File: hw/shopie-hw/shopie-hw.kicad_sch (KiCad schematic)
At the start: 4 parts, among them J1 Jack-DC, SW1 SW_SPDT

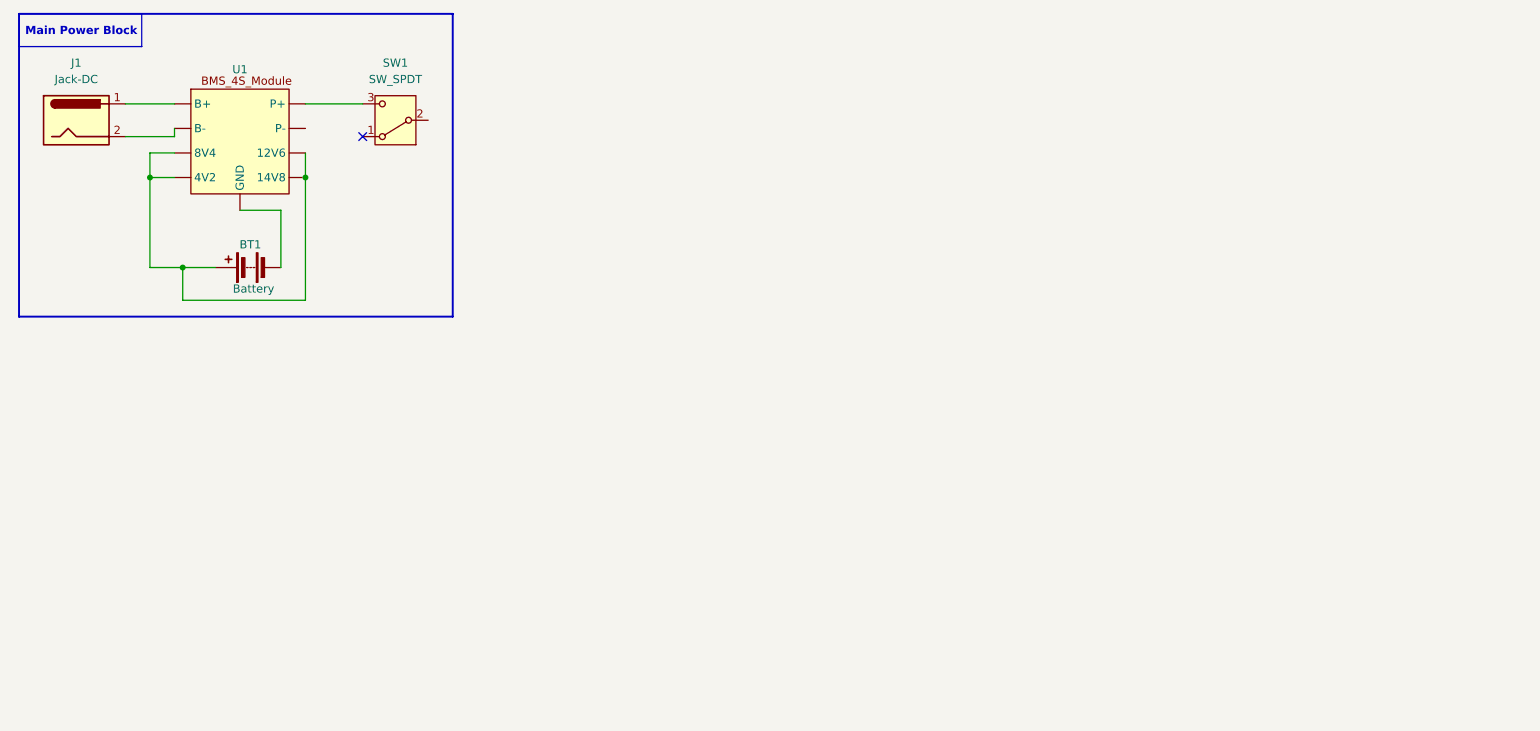
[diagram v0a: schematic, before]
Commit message: Add 5V and 3.3V voltage regulators to main power block
- Added switching regulator for 5V generation from VBAT
- Added LDO regulator for 3.3V output from 5V
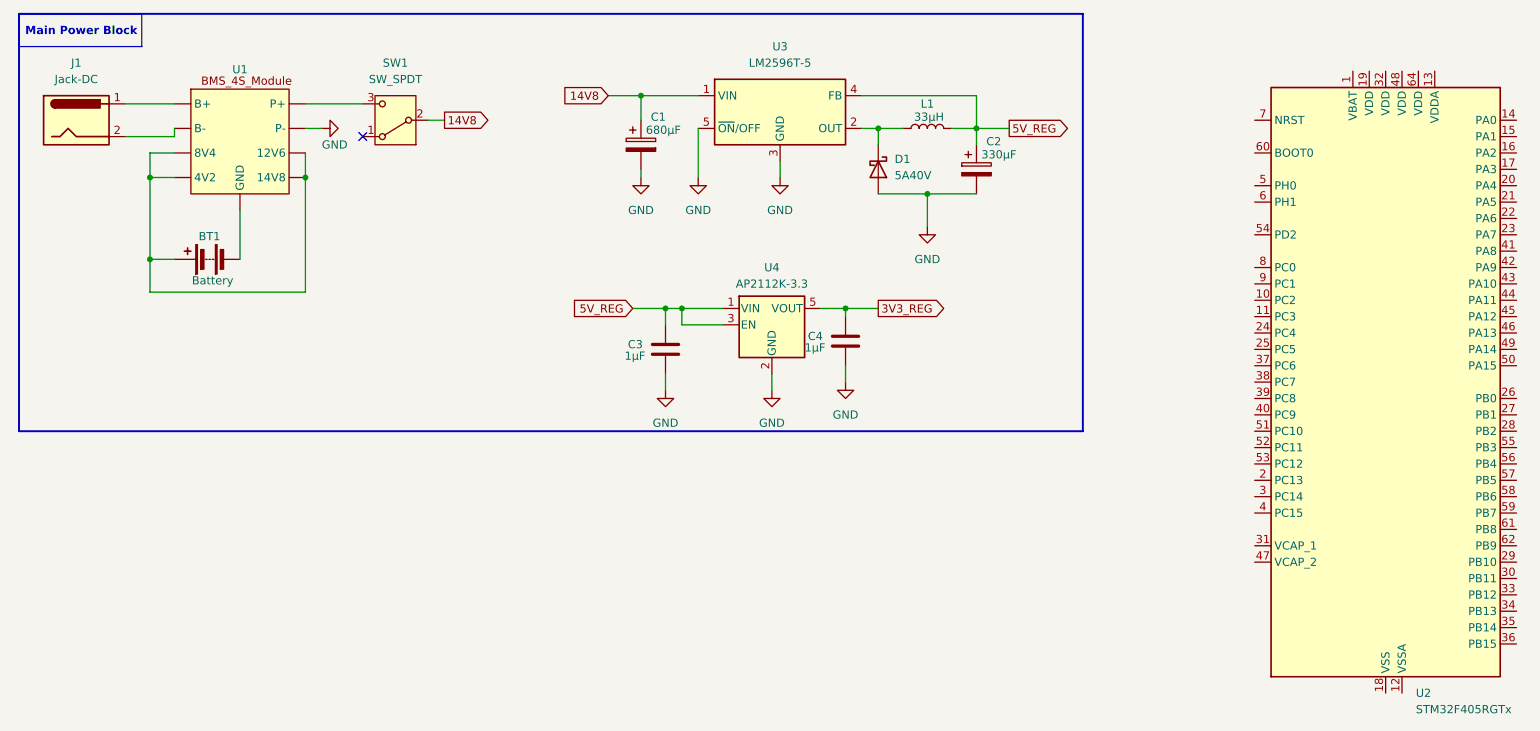
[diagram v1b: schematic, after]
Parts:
- added C1: 680µF, symbol Device:C_Polarized
- added C2: 330µF, symbol Device:C_Polarized
- added C3, C4: 1µF, symbol Device:C
- added D1: 5A40V, symbol Device:D_Schottky
- added L1: 33µH, symbol Device:L
- added U2: STM32F405RGTx, Package_QFP:LQFP-64_10x10mm_P0.5mm, symbol MCU_ST_STM32F4:STM32F405RGTx
- added U3: LM2596T-5, Package_TO_SOT_THT:TO-220-5_P3.4x3.7mm_StaggerOdd_Lead3.8mm_Vertical, symbol Regulator_Switching:LM2596T-5
- added U4: AP2112K-3.3, Package_TO_SOT_SMD:SOT-23-5, symbol Regulator_Linear:AP2112K-3.3
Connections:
- net GND: now reaches U1. (14V8)
- net GND: now also C1.2, C2.2, C3.2, C4.2, D1.2 (A), U3.3 (GND), U3.5 (~{ON}/OFF), U4.2 (GND)
- net 14V8: now reaches SW1.2 (B)
- net 14V8: now also C1.1, U3.1 (VIN)
- new net: D1.1 (K), L1.1, U3.2 (OUT)
- new net: U2.18 (VSS), U2.63 (VSS)
- new net 3V3_REG: C4.1, U4.5 (VOUT)
- new net 5V_REG: C2.1, C3.1, L1.2, U3.4 (FB), U4.1 (VIN), U4.3 (EN)
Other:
- moved on the sheet: BT1

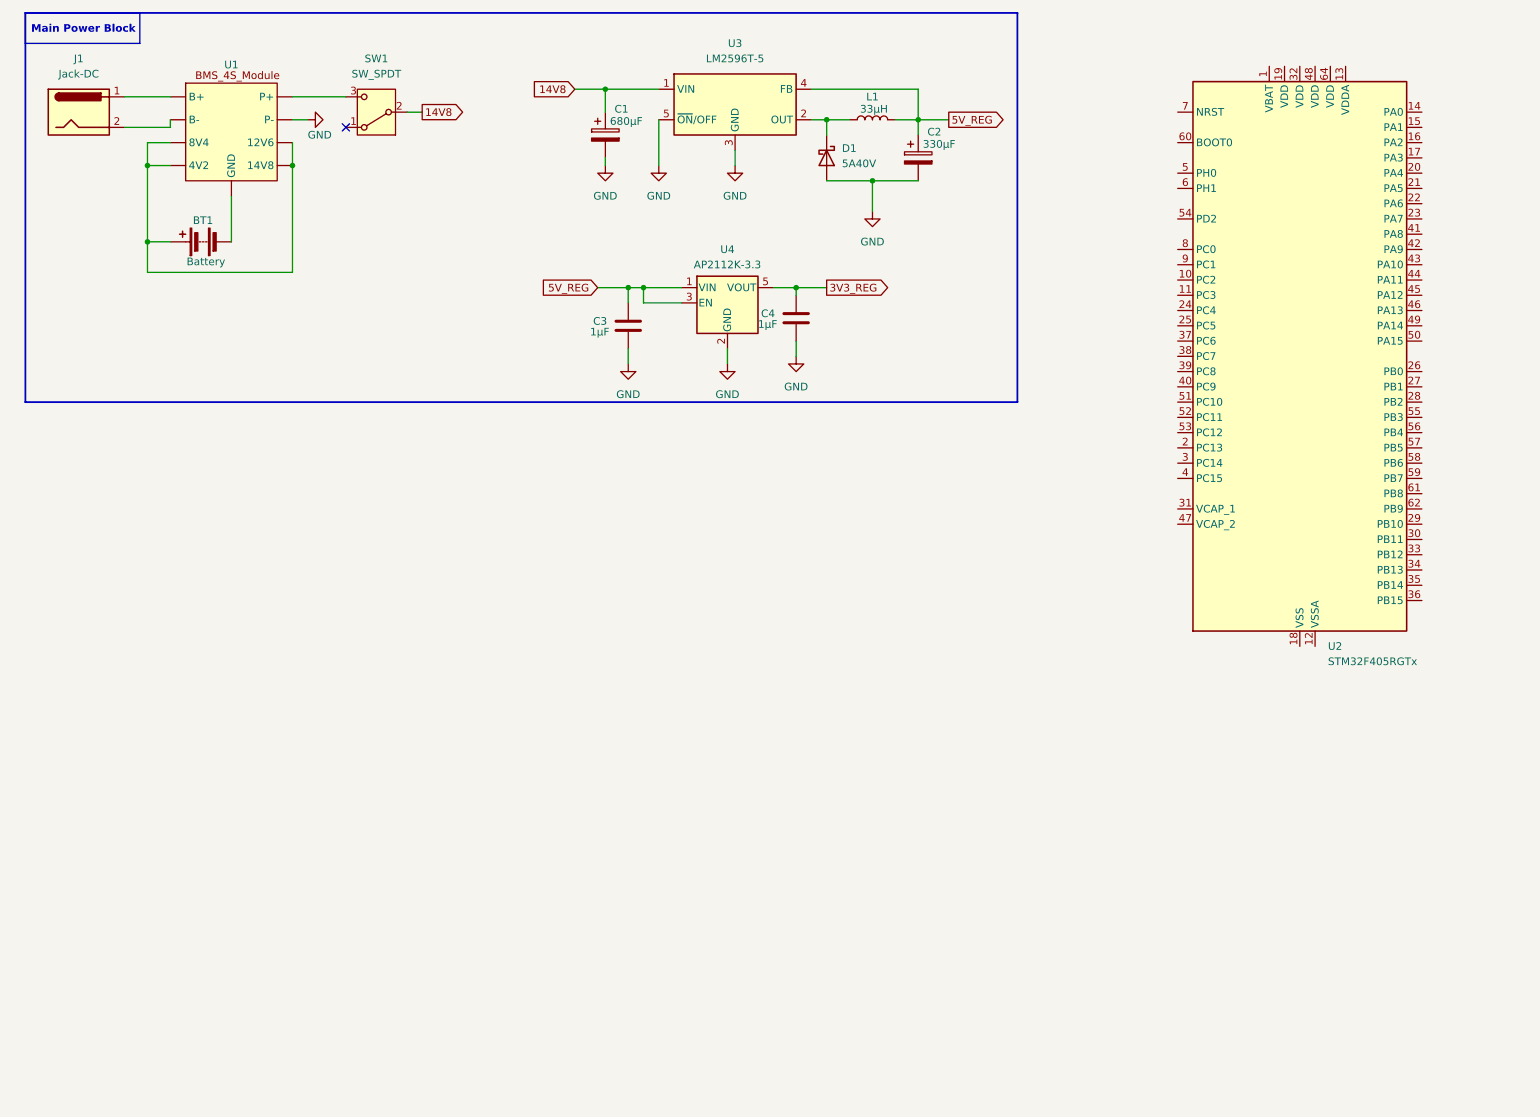
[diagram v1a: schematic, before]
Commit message: Add MCU power, ground, VCAPS, reset button, and BOOT0 toggle switch connections
- Connected VDD and VDDA pins to 3.3V supply

- Connected VSS and VSSA pins to ground

- Added VCAPS capacitors for internal regulator

- Added NRST pin reset circuit with tact push button

- Added BOOT0 pin with toggle switch for boot mode selection
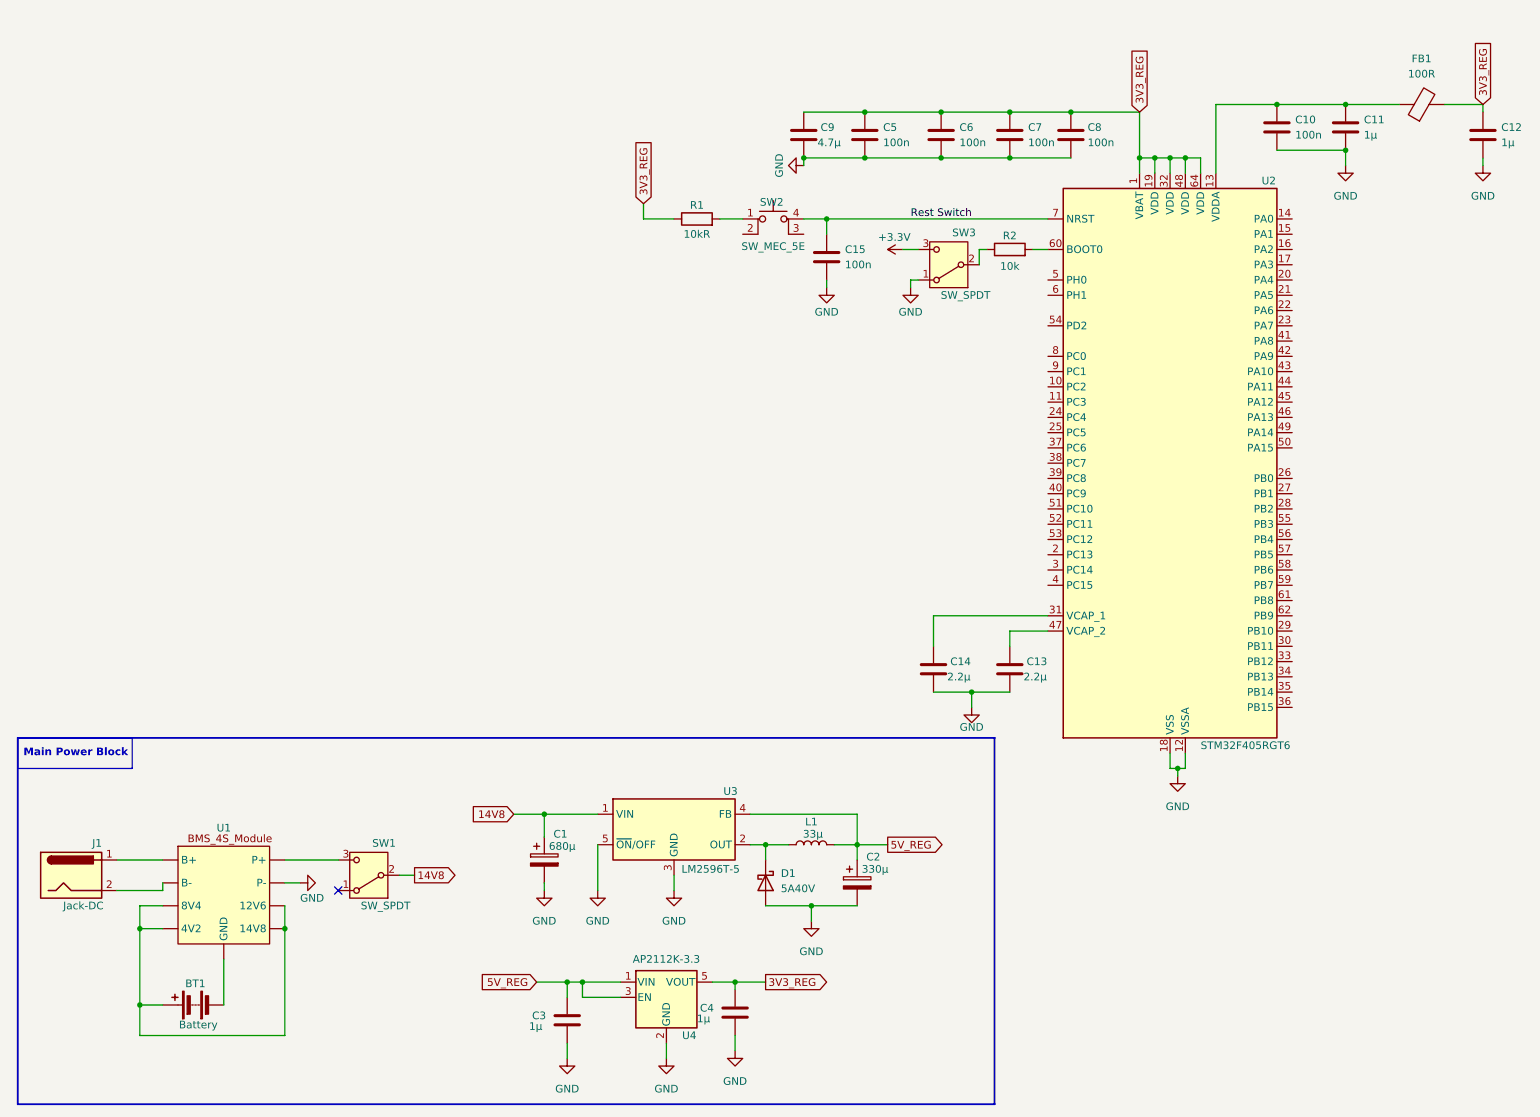
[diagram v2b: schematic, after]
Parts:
- added C10, C15, C5, C6, C7, C8: 100n, symbol Device:C
- added C11, C12: 1µ, symbol Device:C
- added C13, C14: 2.2µ, symbol Device:C
- added C9: 4.7µ, symbol Device:C
- added FB1: 100R, symbol Device:FerriteBead
- added R1: 10kR, symbol Device:R
- added R2: 10k, symbol Device:R
- added SW2: SW_MEC_5E, symbol Switch:SW_MEC_5E
- added SW3: SW_SPDT, symbol Switch:SW_SPDT
- C1: value 680µF -> 680µ
- C2: value 330µF -> 330µ
- C3, C4: value 1µF -> 1µ
- L1: value 33µH -> 33µ
- U2: value STM32F405RGTx -> STM32F405RGT6
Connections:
- net 3V3_REG: now also U2.1 (VBAT), U2.19 (VDD), U2.32 (VDD), U2.48 (VDD), U2.64 (VDD), C12.1, C5.1, C6.1, C7.1, C8.1, C9.1, FB1.2, R1.1
- net GND: now also U2.12 (VSSA), U2.18 (VSS), U2.63 (VSS), C10.2, C11.2, C12.2, C13.2, C14.2, C15.2, C5.2, C6.2, C7.2, C8.2, C9.2, SW3.1 (A)
- net at U2.13 (VDDA): now also C10.1, C11.1, FB1.1
- net at U2.31 (VCAP_1): now also C14.1
- net at U2.47 (VCAP_2): now also C13.1
- net at U2.60 (BOOT0): now also R2.2
- net Rest Switch: now reaches U2.7 (NRST)
- net Rest Switch: now also C15.1, SW2.4 (A)
- new net: R1.2, SW2.1
- new net: R2.1, SW3.2 (B)
- new net +3.3V: SW3.3 (C)
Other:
- moved on the sheet: BT1, C1, C2, C3, C4, D1, J1, L1, SW1, U1, U2, U3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
